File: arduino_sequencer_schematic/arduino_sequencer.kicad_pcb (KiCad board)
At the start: 2 copper layers, 296 x 178 mm, 178 parts, among them J1 AudioJack, J10 AudioJack, J11 AudioJack, J12 AudioJack, J13 AudioJack, J14 AudioJack, J15 AudioJack, J16 Conn_02x05, J17 Conn_01x03, J2 AudioJack, J3 AudioJack, J4 AudioJack, J5 AudioJack, J6 AudioJack, J7 AudioJack, J8 AudioJack, J9 AudioJack, Q1 2N3904, Q10 2N3904, Q11 2N3904, Q2 2N3904, Q3 2N3904, Q4 2N3904, Q5 2N3904, Q6 2N3904, Q7 2N3904, Q8 2N3904, Q9 2N3904, SW1 SW_SPST, SW2 SW_Push, SW3 SW_Push, SW4 SW_Push, SW5 SW_SPST, SW6 SW_SPST, U1 L78L09_TO92, U2 74HC595, U3 TL084, U4 TL084, U5 L7805

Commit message: Added resistor values on silkscreen
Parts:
- R1, R10, R11, R12, R13, R14, R15, R16, R17, R18, R19, R2, R20, R21, R22, R23, R24, R25, R26, R27, R28, R29, R3, R30, R31, R32, R33, R34, R35, R36, R37, R38, R39, R4, R40, R41, R42, R43, R44, R45, R46, R47, R48, R49, R5, R50, R51, R52, R53, R54, R55, R56, R57, R58, R59, R6, R60, R61, R62, R63, R64, R65, R66, R7, R8, R9: footprint Resistor_THT:R_Axial_DIN0207_L6.3mm_D2.5mm_P10.16mm_Horizontal -> TimMJN:R_Axial_DIN0207_L6.3mm_D2.5mm_P10.16mm_Horizontal_Value_SilkS

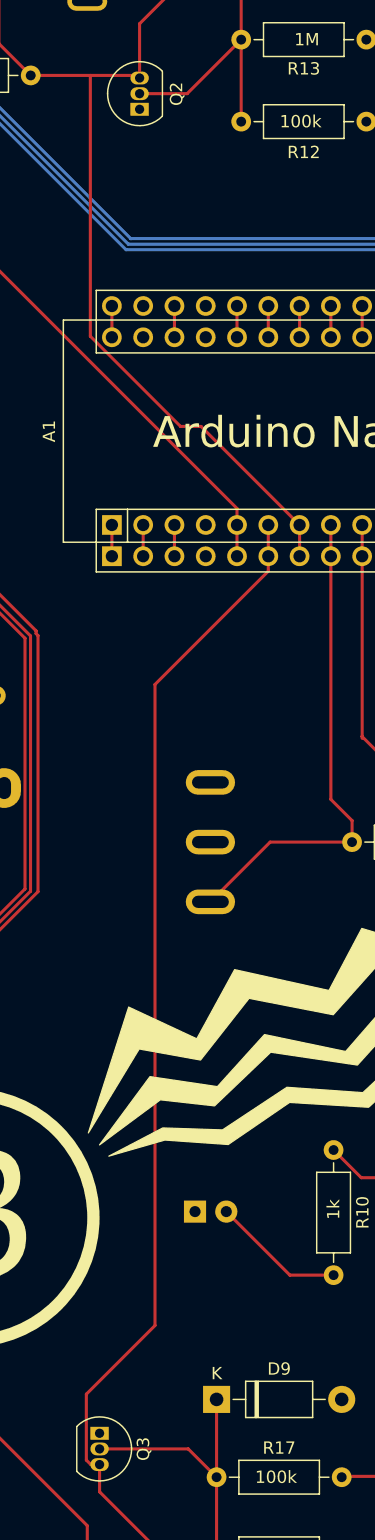
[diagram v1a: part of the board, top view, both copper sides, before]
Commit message: fixed arduino reset/flip pin inconsistency
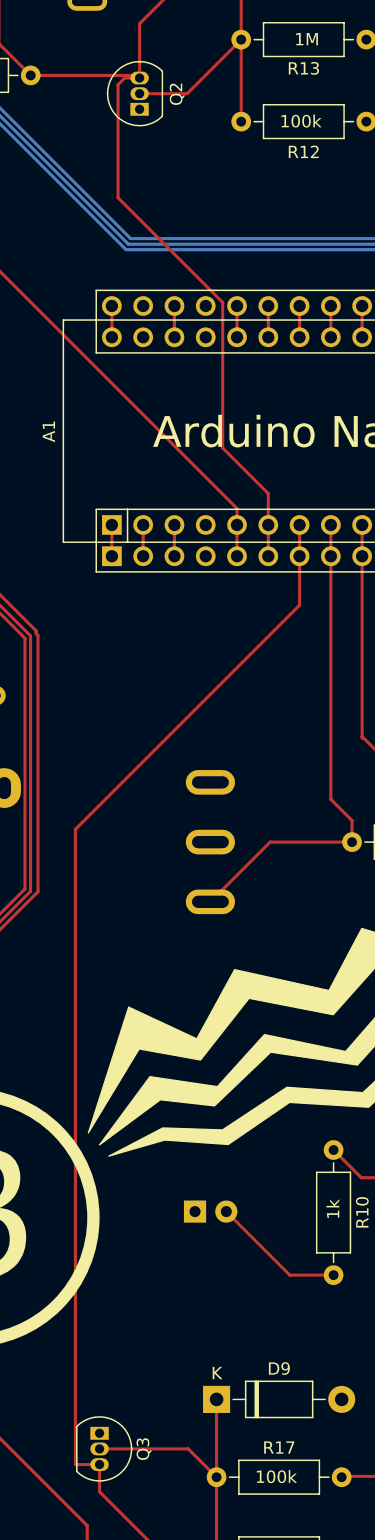
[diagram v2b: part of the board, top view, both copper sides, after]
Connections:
- A1 pad 6: FLIP_IN -> RESET_IN
- A1 pad 7: RESET_IN -> FLIP_IN
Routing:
- net FLIP_IN: track 155.8 -> 158.3 mm
- net RESET_IN: track 111.4 -> 109.7 mm

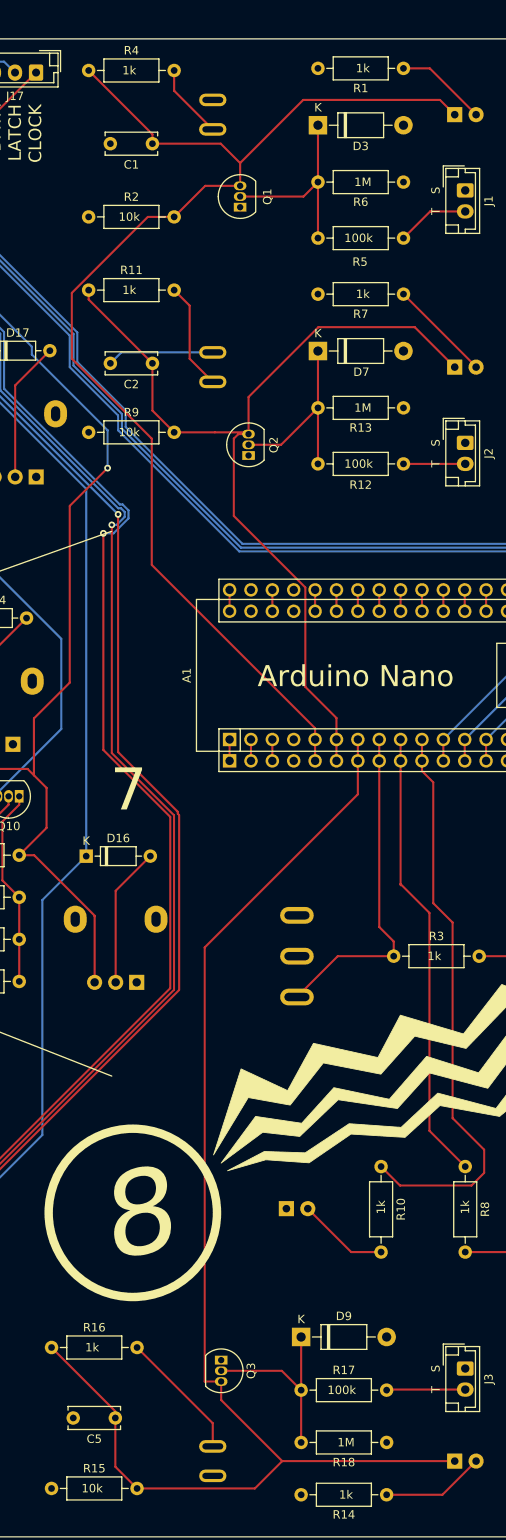
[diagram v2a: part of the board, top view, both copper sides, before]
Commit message: Move filter resistor
For improved stability (no faulty triggers)
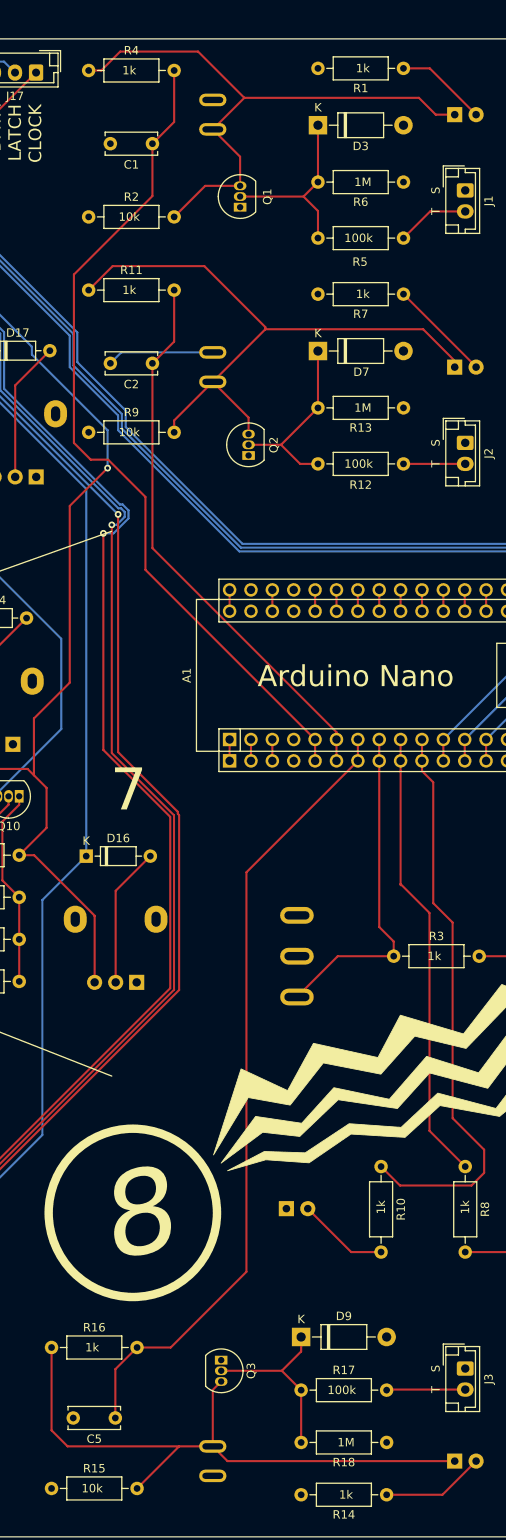
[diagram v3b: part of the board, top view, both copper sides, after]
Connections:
- D2 pad 1: CLOCK_IN -> Net-(D2-Pad1)
- D5 pad 1: RESET_IN -> Net-(D5-Pad1)
- D8 pad 1: FLIP_IN -> Net-(D8-Pad1)
- Q1 pad 3: CLOCK_IN -> Net-(D2-Pad1)
- Q2 pad 3: RESET_IN -> Net-(D5-Pad1)
- Q3 pad 3: FLIP_IN -> Net-(D8-Pad1)
- R11 pad 1: RESET_IN -> Net-(D5-Pad1)
- R11 pad 2: Net-(R11-Pad2) -> RESET_IN
- R15 pad 2: FLIP_IN -> Net-(D8-Pad1)
- R16 pad 1: FLIP_IN -> Net-(D8-Pad1)
- R16 pad 2: Net-(R16-Pad2) -> FLIP_IN
- R2 pad 2: CLOCK_IN -> Net-(D2-Pad1)
- R4 pad 1: CLOCK_IN -> Net-(D2-Pad1)
- R4 pad 2: Net-(R4-Pad2) -> CLOCK_IN
- R9 pad 2: RESET_IN -> Net-(D5-Pad1)
- SW2 pad 1: Net-(R4-Pad2) -> Net-(D2-Pad1)
- SW3 pad 1: Net-(R11-Pad2) -> Net-(D5-Pad1)
- SW4 pad 1: Net-(R16-Pad2) -> Net-(D8-Pad1)
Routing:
- net Net-(D5-Pad1): track 0.00 -> 74.9 mm
- net Net-(D8-Pad1): track 0.00 -> 74.5 mm
- net Net-(D2-Pad1): track 0.00 -> 70.3 mm
- net FLIP_IN: track 158.3 -> 94.9 mm
- net CLOCK_IN: track 148.1 -> 100.1 mm
- net RESET_IN: track 109.7 -> 66.1 mm
- net Net-(R16-Pad2): track 15.5 -> 0.00 mm
- net Net-(R11-Pad2): track 12.8 -> 0.00 mm
- net Net-(R4-Pad2): track 8.90 -> 0.00 mm
- net Net-(D9-Pad1): track 23.0 -> 21.6 mm
- net Net-(D7-Pad1): track 23.5 -> 22.2 mm
- net Net-(D3-Pad1): track 23.4 -> 22.4 mm

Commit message: Finetuned gain/offset ranges
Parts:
- R20, R59: value 10k -> 47k
- R22, R61: value 10k -> 100k
- RV18, RV21: value B50k -> B100k
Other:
- board text added: "07-01-2021"
- board text removed: "30-12-2020"

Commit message: Date update
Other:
- board text added: "30-12-2020"
- board text removed: "07-01-2021"
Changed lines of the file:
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@@
     (46 B.CrtYd user hide)
     (47 F.CrtYd user hide)
-    (48 B.Fab user hide)
+    (48 B.Fab user)
     (49 F.Fab user hide)
   )
@@
     (effects (font (size 2 2) (thickness 0.3)))
   )
-  (gr_text 07-01-2021 (at 344 118) (layer F.SilkS)
+  (gr_text 30-12-2020 (at 344 118) (layer F.SilkS)
     (effects (font (size 1.5 1.5) (thickness 0.15)))
   )

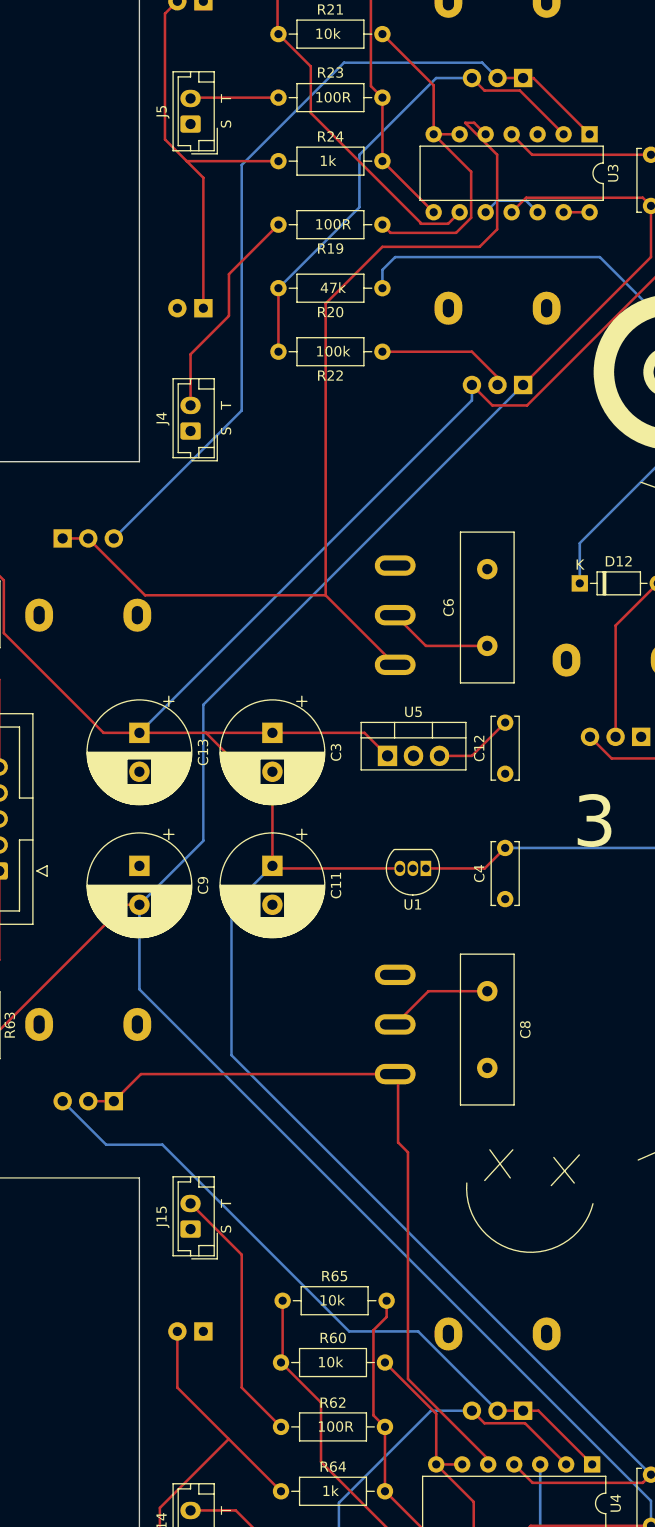
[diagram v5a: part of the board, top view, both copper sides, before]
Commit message: Fixed potentiometer directions
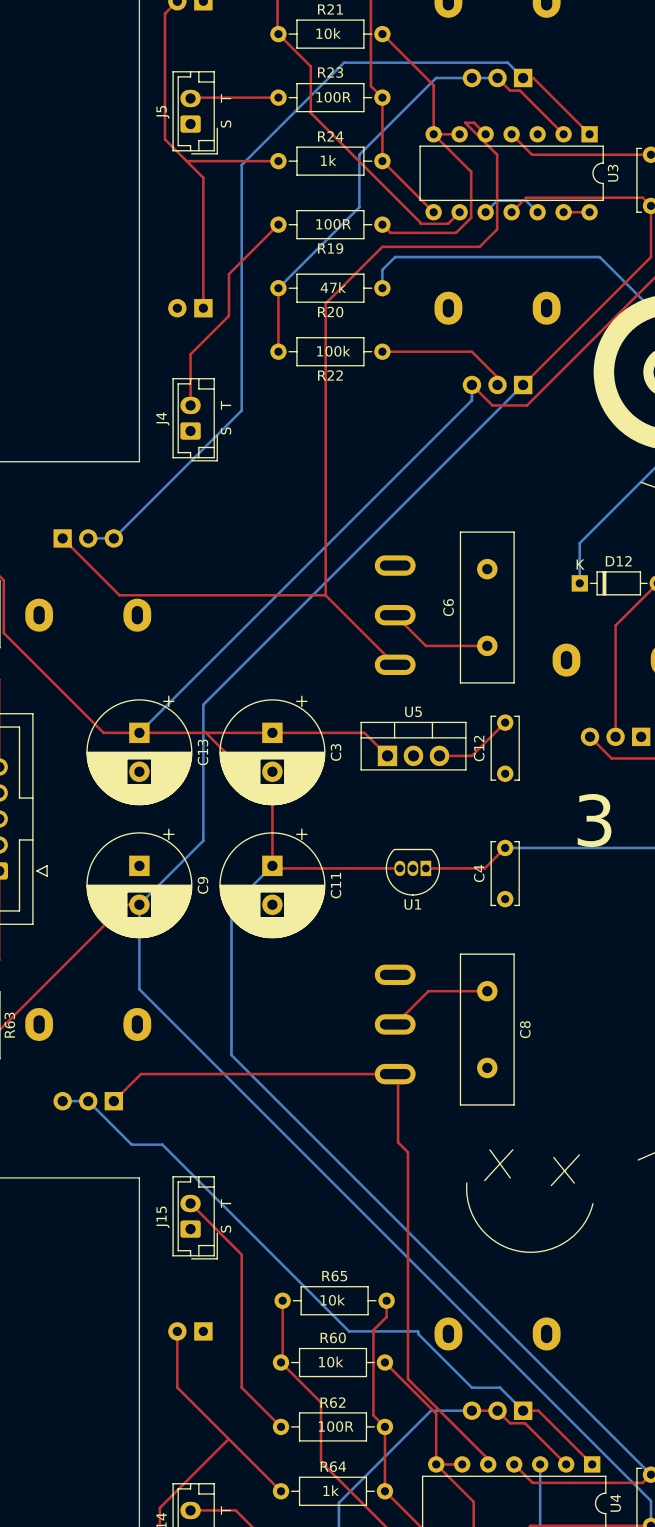
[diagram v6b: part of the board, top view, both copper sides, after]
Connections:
- RV17 pad 2: Net-(RV17-Pad1) -> Net-(RV17-Pad2)
- RV17 pad 3: Net-(RV17-Pad3) -> Net-(RV17-Pad2)
- RV18 pad 1: Net-(RV17-Pad3) -> Net-(RV17-Pad2)
- RV18 pad 2: Net-(RV17-Pad3) -> Net-(R20-Pad2)
- RV20 pad 2: Net-(RV20-Pad1) -> Net-(RV20-Pad2)
- RV20 pad 3: Net-(RV20-Pad3) -> Net-(RV20-Pad2)
- RV21 pad 1: Net-(RV20-Pad3) -> Net-(RV20-Pad2)
- RV21 pad 2: Net-(RV20-Pad3) -> Net-(R59-Pad2)
- U3 pad 1: Net-(RV17-Pad3) -> Net-(RV17-Pad2)
- U4 pad 1: Net-(RV20-Pad3) -> Net-(RV20-Pad2)
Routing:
- net Net-(RV17-Pad2): track 0.00 -> 85.2 mm
- net Net-(RV17-Pad3): track 82.7 -> 0.00 mm
- net Net-(RV20-Pad2): track 0.00 -> 66.6 mm
- net Net-(RV20-Pad3): track 66.5 -> 0.00 mm
- net Net-(RV20-Pad1): track 73.0 -> 70.5 mm

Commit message: prepare for production
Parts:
- added REF**: MountingHole_3.2mm_M3, MountingHole:MountingHole_3.2mm_M3, F.Cu at (62.0, 181.0)
- added REF**: MountingHole_3.2mm_M3, MountingHole:MountingHole_3.2mm_M3, F.Cu at (62.0, 121.0)
- added REF**: MountingHole_3.2mm_M3, MountingHole:MountingHole_3.2mm_M3, F.Cu at (348.0, 121.0)
- added REF**: MountingHole_3.2mm_M3, MountingHole:MountingHole_3.2mm_M3, F.Cu at (348.0, 211.0)
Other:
- board text added: "08-01-2021"
- board text added: "Panel backside"
- board text removed: "30-12-2020"
